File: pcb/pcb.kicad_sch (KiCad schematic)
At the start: 100 parts, among them SW1 SW_Push_45deg, SW10 SW_Push_45deg, SW11 SW_Push_45deg, SW12 SW_Push_45deg, SW13 SW_Push_45deg, SW14 SW_Push_45deg, SW15 SW_Push_45deg, SW16 SW_Push_45deg, SW17 SW_Push_45deg, SW18 SW_Push_45deg, SW19 SW_Push_45deg, SW2 SW_Push_45deg, SW20 SW_Push_45deg, SW21 SW_Push_45deg, SW22 SW_Push_45deg, SW23 SW_Push_45deg, SW24 SW_Push_45deg, SW25 SW_Push_45deg, SW26 SW_Push_45deg, SW27 SW_Push_45deg, SW28 SW_Push_45deg, SW29 SW_Push_45deg, SW3 SW_Push_45deg, SW30 SW_Push_45deg, SW31 SW_Push_45deg, SW32 SW_Push_45deg, SW33 SW_Push_45deg, SW34 SW_Push_45deg, SW35 SW_Push_45deg, SW36 SW_Push_45deg, SW37 SW_Push_45deg, SW38 SW_Push_45deg, SW39 SW_Push_45deg, SW4 SW_Push_45deg, SW40 SW_Push_45deg, SW41 SW_Push_45deg, SW42 SW_Push_45deg, SW43 SW_Push_45deg, SW44 SW_Push_45deg, SW45 SW_Push_45deg, SW46 SW_Push_45deg, SW47 SW_Push_45deg, SW48 SW_Push_45deg, SW49 SW_Push_45deg, SW5 SW_Push_45deg, SW50 SW_Push_45deg, SW6 SW_Push_45deg, SW7 SW_Push_45deg, SW8 SW_Push_45deg, SW9 SW_Push_45deg

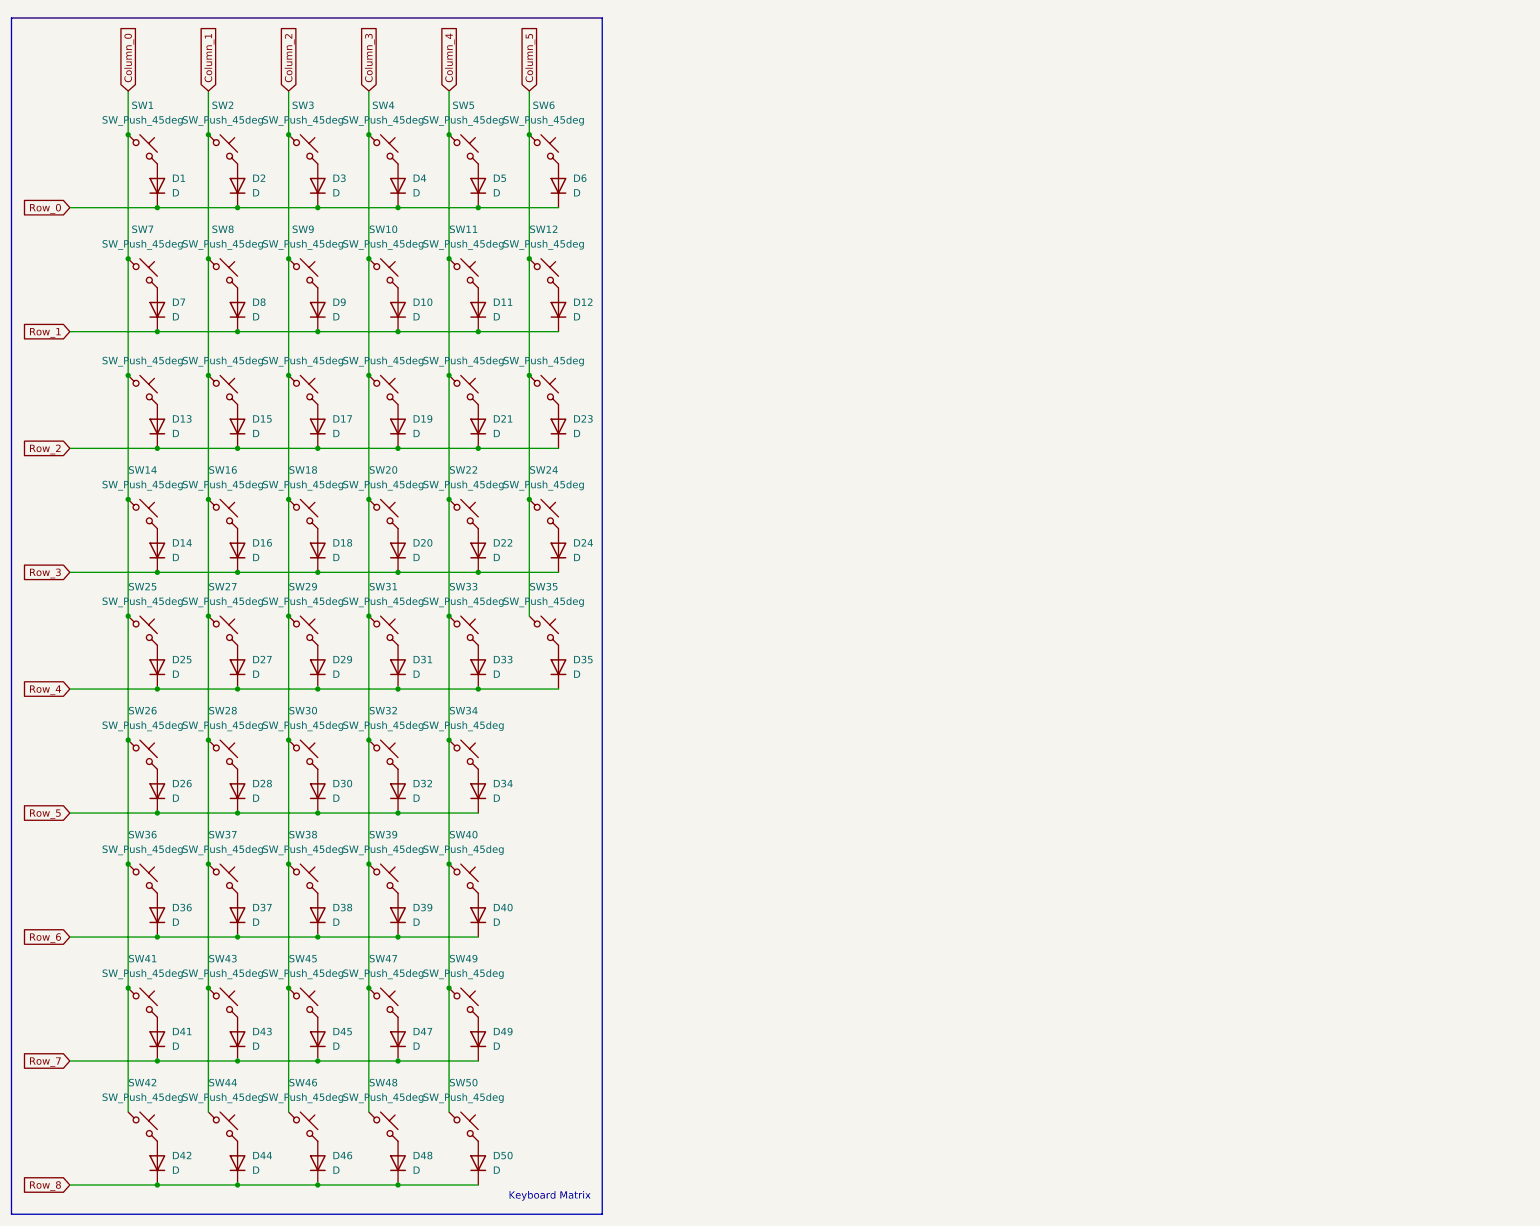
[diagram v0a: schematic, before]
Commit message: [Hardware] Add debug port and external MCU circuitry
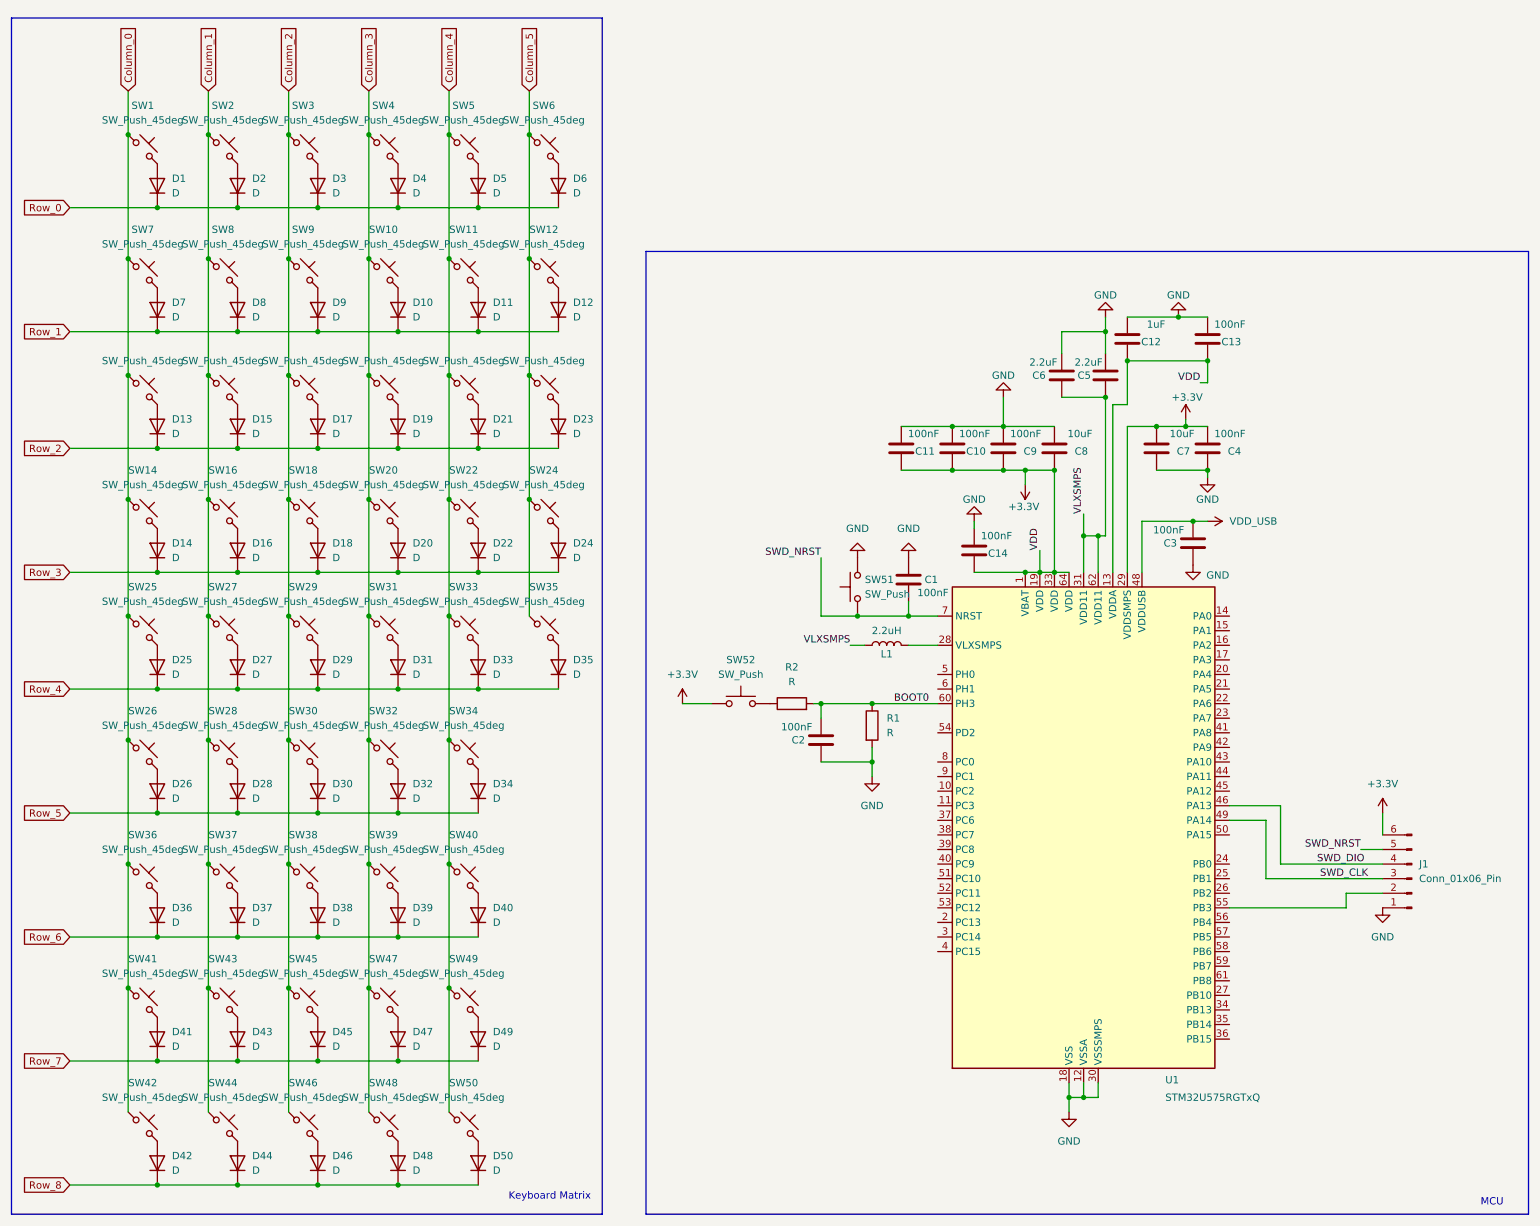
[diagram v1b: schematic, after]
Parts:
- added C1, C10, C11, C13, C14, C2, C3, C4, C9: 100nF, symbol Device:C
- added C12: 1uF, symbol Device:C
- added C5, C6: 2.2uF, symbol Device:C
- added C7, C8: 10uF, symbol Device:C
- added J1: Conn_01x06_Pin, symbol Connector:Conn_01x06_Pin
- added L1: 2.2uH, symbol Device:L
- added R1, R2: R, symbol Device:R
- added SW51, SW52: SW_Push, symbol Switch:SW_Push
- added U1: STM32U575RGTxQ, Package_QFP:LQFP-64_10x10mm_P0.5mm, symbol MCU_ST_STM32U5:STM32U575RGTxQ
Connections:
- new net: L1.2, U1.28 (VLXSMPS)
- new net: R2.1, SW52.2
- new net: J1.2 (Pin_2), U1.55 (PB3)
- new net +3.3V: C10.1, C11.1, C12.1, C13.1, C14.1, C4.2, C7.2, C8.1, C9.1, J1.6 (Pin_6), SW52.1, U1.1 (VBAT), U1.13 (VDDA), U1.19 (VDD), U1.29 (VDDSMPS), U1.33 (VDD), U1.64 (VDD)
- new net BOOT0: C2.2, R1.1, R2.2, U1.60 (PH3)
- new net GND: C1.1, C10.2, C11.2, C12.2, C13.2, C14.2, C2.1, C3.1, C4.1, C5.2, C6.2, C7.1, C8.2, C9.2, J1.1 (Pin_1), R1.2, SW51.2, U1.12 (VSSA), U1.18 (VSS), U1.30 (VSSSMPS), U1.32 (VSS), U1.47 (VSS), U1.63 (VSS)
- new net SWD_CLK: J1.3 (Pin_3), U1.49 (PA14)
- new net SWD_DIO: J1.4 (Pin_4), U1.46 (PA13)
- new net SWD_NRST: C1.2, J1.5 (Pin_5), SW51.1, U1.7 (NRST)
- new net VDD_USB: C3.2, U1.48 (VDDUSB)
- new net VLXSMPS: C5.1, C6.1, L1.1, U1.31 (VDD11), U1.62 (VDD11)
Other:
- note added: "MCU"
